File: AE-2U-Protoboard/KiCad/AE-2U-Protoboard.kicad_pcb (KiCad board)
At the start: 4 copper layers, 50 x 100 mm, 721 parts

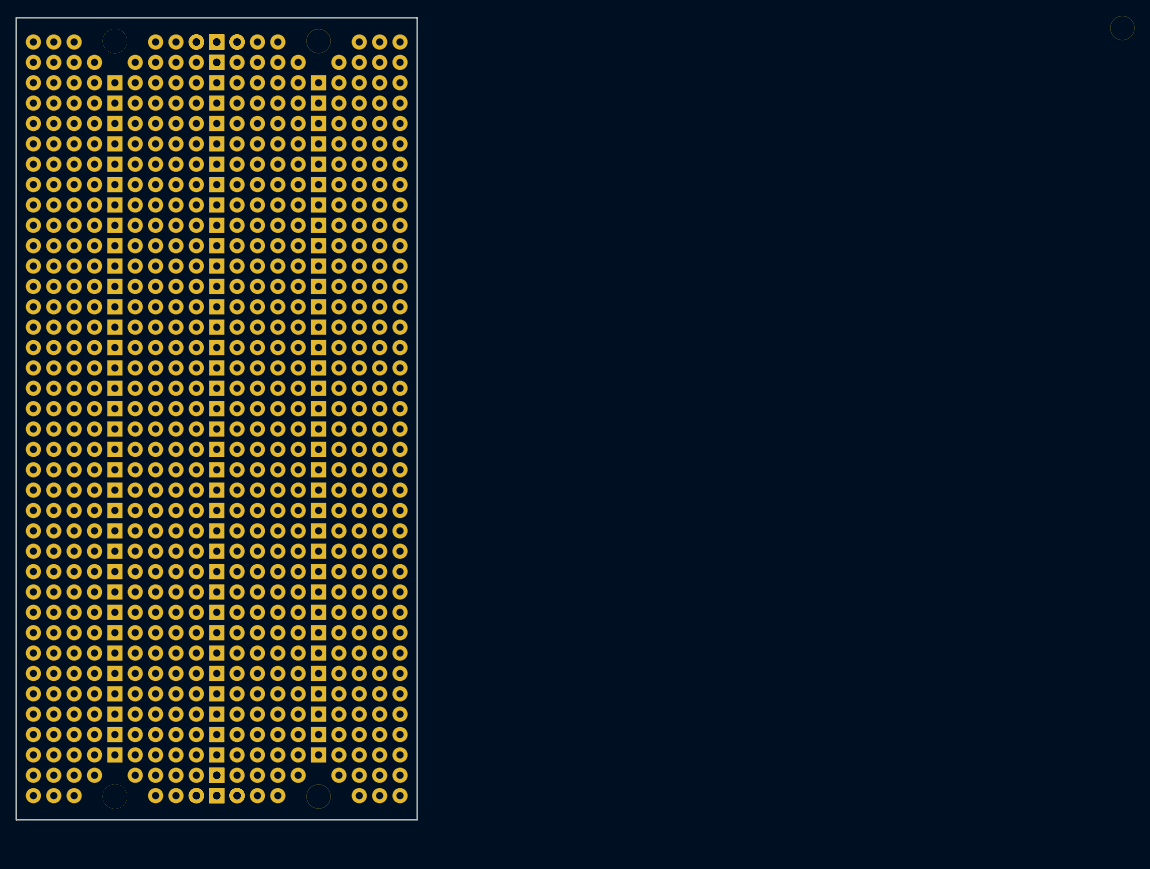
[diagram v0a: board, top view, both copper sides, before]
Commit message: added logo and copyright messages
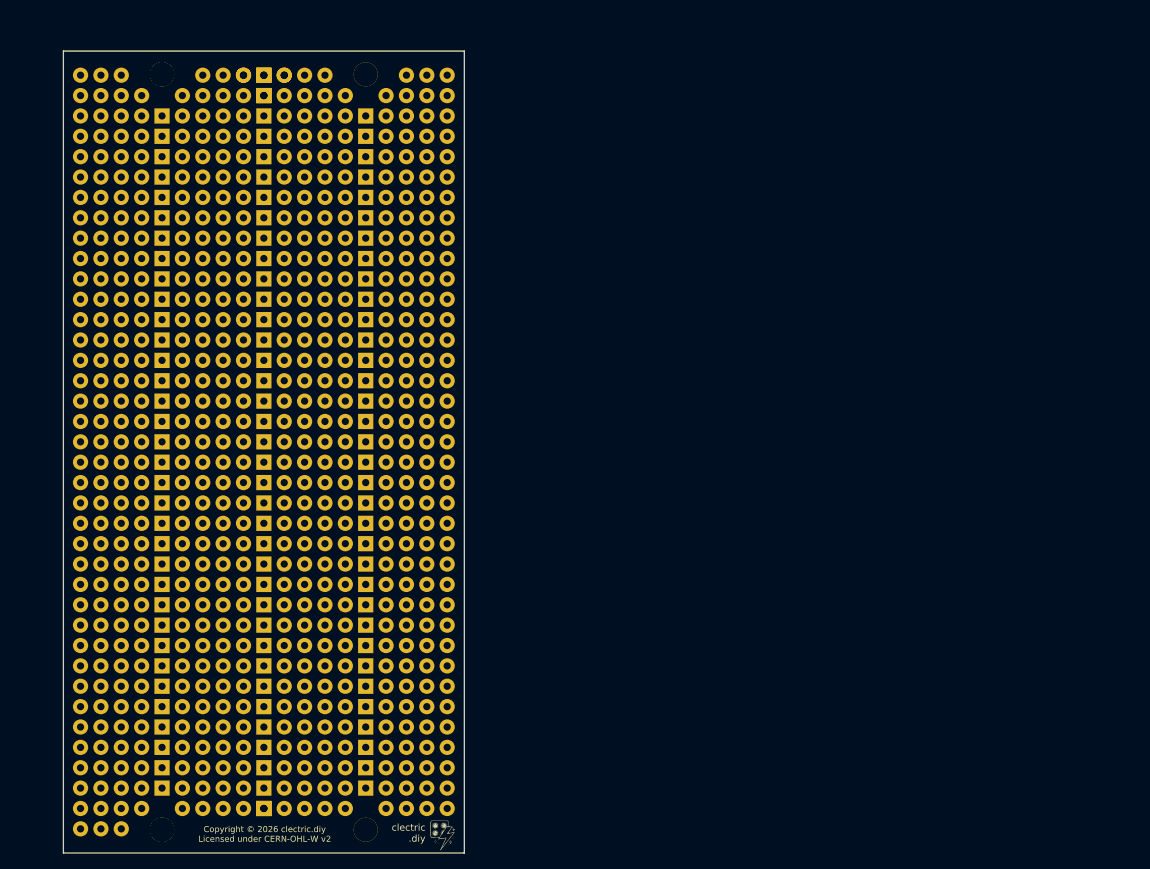
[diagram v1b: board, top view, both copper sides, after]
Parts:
- removed the ? at (105.1, 145.1)
- removed the ? at (110.2, 145.1)
- removed the ? at (107.6, 145.1)
- removed the REF** at (107.6, 145.1)
- removed the REF** at (127.9, 145.1)
- removed the REF** at (127.9, 142.6)
- removed the REF** at (100.0, 145.1)
- removed the REF** at (130.5, 145.1)
- removed the REF** at (130.5, 142.6)
- removed the REF** at (105.1, 145.1)
- removed the REF** at (115.2, 145.1)
- removed the REF** at (125.4, 145.1)
- removed the REF** at (122.8, 142.6)
- removed the REF** at (112.7, 145.1)
- removed the REF** at (125.4, 142.6)
- removed the REF** at (110.2, 145.1)
- removed the REF** at (220.6, 49.4)
- removed the REF** at (102.5, 145.1)
- added G***: LOGO, LOGO, F.Cu at (135.7, 150.1)
- added REF**: Pad, clectric-diy:Pad, F.Cu at (136.3, 146.7)
- added REF**: Pad, clectric-diy:Pad, F.Cu at (133.8, 146.7)
- added REF**: Pad, clectric-diy:Pad, F.Cu at (128.7, 146.7)
- added REF**: Pad, clectric-diy:Pad, F.Cu at (131.3, 146.7)
- moved REF** 7.19 mm to (105.9, 134.0)
- moved REF** 7.19 mm to (100.8, 131.5)
- moved REF** 7.19 mm to (123.7, 141.7)
- moved REF** 7.19 mm to (131.3, 139.1)
- moved REF** 7.19 mm to (123.7, 131.5)
- moved REF** 7.19 mm to (105.9, 141.7)
- moved REF** 7.19 mm to (131.3, 131.5)
- moved REF** 7.19 mm to (123.7, 134.0)
- moved REF** 7.19 mm to (105.9, 131.5)
- moved REF** 7.19 mm to (100.8, 134.0)
- moved REF** 7.19 mm to (131.3, 134.0)
- moved REF** 7.19 mm to (131.3, 141.7)
- moved REF** 7.19 mm to (105.9, 139.1)
- moved REF** 7.19 mm to (111.0, 139.1)
- moved REF** 7.19 mm to (123.7, 139.1)
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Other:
- board text added: "Copyright © 2026 clectric.diy Licensed under CERN-OHL-W v2"
- board text added: "clectric .diy"

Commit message: removed extra layers that were unintentionally added
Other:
- copper layers 4 -> 2
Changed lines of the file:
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@@
 	(layers
 		(0 "F.Cu" signal "Front")
-		(4 "In1.Cu" signal)
-		(6 "In2.Cu" signal)
 		(2 "B.Cu" signal "Back")
 		(13 "F.Paste" user)
@@
 			(layer "dielectric 1"
 				(type "core")
-				(thickness 0.480066)
-				(material "FR4")
-				(epsilon_r 4.5)
-				(loss_tangent 0.02)
-			)
-			(layer "In1.Cu"
-				(type "copper")
-				(thickness 0.035)
-			)
-			(layer "dielectric 2"
-				(type "prepreg")
-				(thickness 0.480066)
-				(material "FR4")
-				(epsilon_r 4.5)
-				(loss_tangent 0.02)
-			)
-			(layer "In2.Cu"
-				(type "copper")
-				(thickness 0.035)
-			)
-			(layer "dielectric 3"
-				(type "core")
-				(thickness 0.480066)
+				(thickness 1.510198)
 				(material "FR4")
 				(epsilon_r 4.5)
@@
 		(allow_soldermask_bridges_in_footprints no)
 		(tenting front back)
-		(grid_origin 85.55 47.67)
+		(grid_origin 88.49 52.28)
 		(pcbplotparams
 			(layerselection 0x00000000_00000000_55555555_5755f5ff)
